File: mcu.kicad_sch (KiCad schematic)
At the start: 0 parts

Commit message: feat(mcu): Add STM32F030F4Px microcontroller to schematic
This commit adds the STM32F030F4Px microcontroller to the `mcu.kicad_sch`
schematic sheet.

- Added the STM32F030F4Px symbol.
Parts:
- added U2: STM32F030F4Px, Package_SO:TSSOP-20_4.4x6.5mm_P0.65mm, symbol MCU_ST_STM32F0:STM32F030F4Px
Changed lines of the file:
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@@
 	(generator_version "9.0")
 	(paper "A4")
+	(symbol
+		(lib_id "MCU_ST_STM32F0:STM32F030F4Px")
+		(at 154.94 105.41 0)
+		(unit 1)
+		(exclude_from_sim no)
+		(in_bom yes)
+		(on_board yes)
+		(dnp no)
+		(fields_autoplaced yes)
+		(property "Reference" "U2"
+			(at 157.0833 125.73 0)
+			(effects
+				(font
+					(size 1.27 1.27)
+				)
+				(justify left)
+			)
+		)
+		(property "Value" "STM32F030F4Px"
+			(at 157.0833 128.27 0)
+			(effects
+				(font
+					(size 1.27 1.27)
+				)
+				(justify left)
+			)
+		)
+		(property "Footprint" "Package_SO:TSSOP-20_4.4x6.5mm_P0.65mm"
+			(at 144.78 123.19 0)
+			(effects
+				(font
+					(size 1.27 1.27)
+				)
+				(justify right)
+				(hide yes)
+			)
+		)
+		(property "Datasheet" "https://www.st.com/resource/en/datasheet/stm32f030f4.pdf"
+			(at 154.94 105.41 0)
+			(effects
+				(font
+					(size 1.27 1.27)
+				)
+				(hide yes)
+			)
+		)
+		(property "Description" "STMicroelectronics Arm Cortex-M0 MCU, 16KB flash, 4KB RAM, 48 MHz, 2.4-3.6V, 15 GPIO, TSSOP20"
+			(at 154.94 105.41 0)
+			(effects
+				(font
+					(size 1.27 1.27)
+				)
+				(hide yes)
+			)
+		)
+		(pin "6"
+		)
+		(pin "7"
+		)
+		(pin "20"
+		)
+		(pin "19"
+		)
+		(pin "5"
+		)
+		(pin "18"
+		)
+		(pin "13"
+		)
+		(pin "9"
+		)
+		(pin "16"
+		)
+		(pin "15"
+		)
+		(pin "3"
+		)
+		(pin "2"
+		)
+		(pin "1"
+		)
+		(pin "4"
+		)
+		(pin "14"
+		)
+		(pin "11"
+		)
+		(pin "17"
+		)
+		(pin "10"
+		)
+		(pin "12"
+		)
+		(pin "8"
+		)
+		(instances
+			(project ""
+				(path "/01550cd7-b424-469c-925b-c370f3609cd4/edb1e4c3-83a3-4443-aa4b-0e758d3bea47"
+					(reference "U2")
+					(unit 1)
+				)
+			)
+		)
+	)
 )

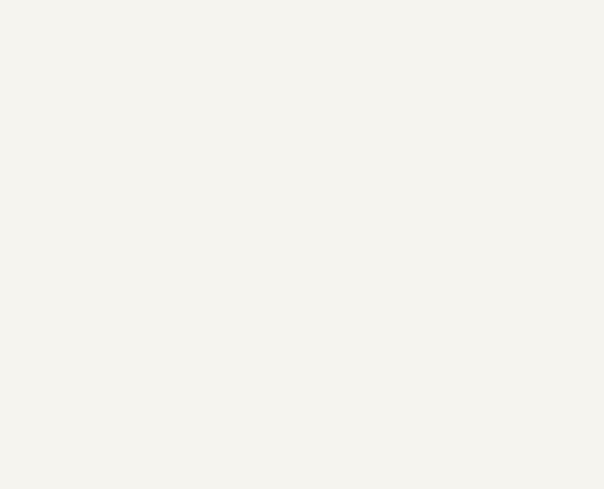
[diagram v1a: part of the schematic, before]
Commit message: feat(power): Added decoupling capacitors for MCU VDD pins
This commit introduces decoupling capacitors on the voltage supply (VDD) pins of
the microcontroller unit (MCU). These capacitors help to stabilize the power
supply by providing a local energy reserve and reducing voltage fluctuations.

This improvement enhances the reliability and stability of the MCU power system,
especially during switching events and periods of high current demand.

Reference

Chapter: 6.1.6 Power supply scheme
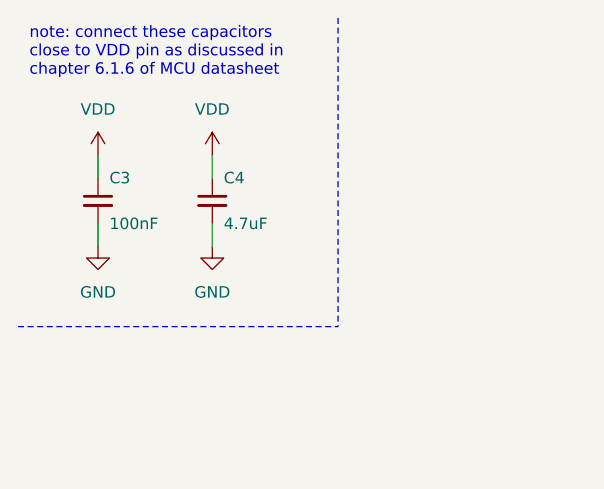
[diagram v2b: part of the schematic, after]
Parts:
- added C3: 100nF, Capacitor_SMD:C_0603_1608Metric_Pad1.08x0.95mm_HandSolder, symbol Device:C_Small
- added C4: 4.7uF, Capacitor_SMD:C_0603_1608Metric_Pad1.08x0.95mm_HandSolder, symbol Device:C_Small
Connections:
- new net GND: C3.2, C4.2
- new net VDD: C3.1, C4.1
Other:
- note added: "note: connect these capacitors close to VDD pin as discussed in chapter 6.1.6 of MCU datasheet"

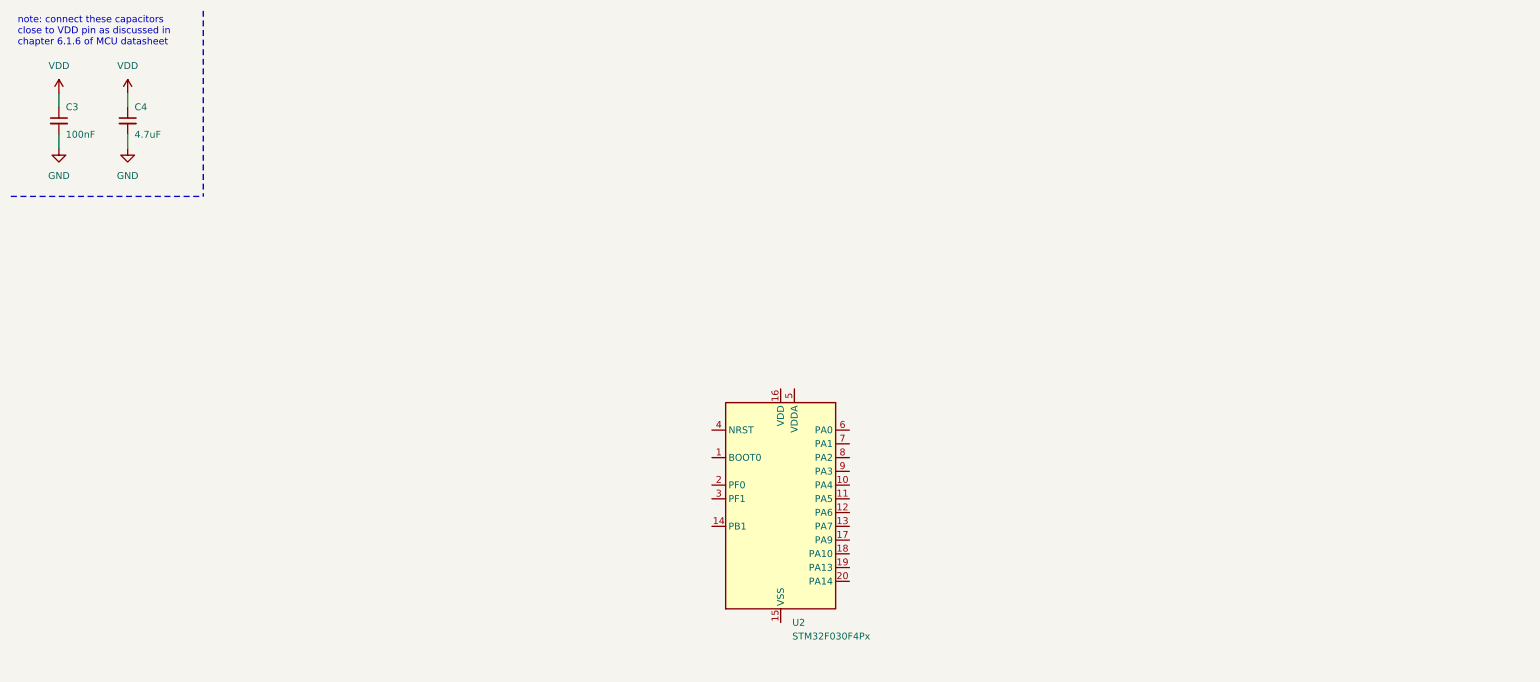
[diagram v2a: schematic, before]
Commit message: feat(power): Added decoupling capacitors for MCU VDDA pins
This commit introduces decoupling capacitors on the analog voltage supply (VDDA)
pins of the microcontroller unit (MCU). Similar to the decoupling for the
digital supply, these capacitors aim to stabilize the analog power rail.

A stable VDDA is crucial for the performance and accuracy of the MCU's analog
peripherals, such as ADCs and DACs. This addition helps to minimize noise and
ensure reliable analog signal processing.

Reference

Chapter: 6.1.6 Power supply scheme
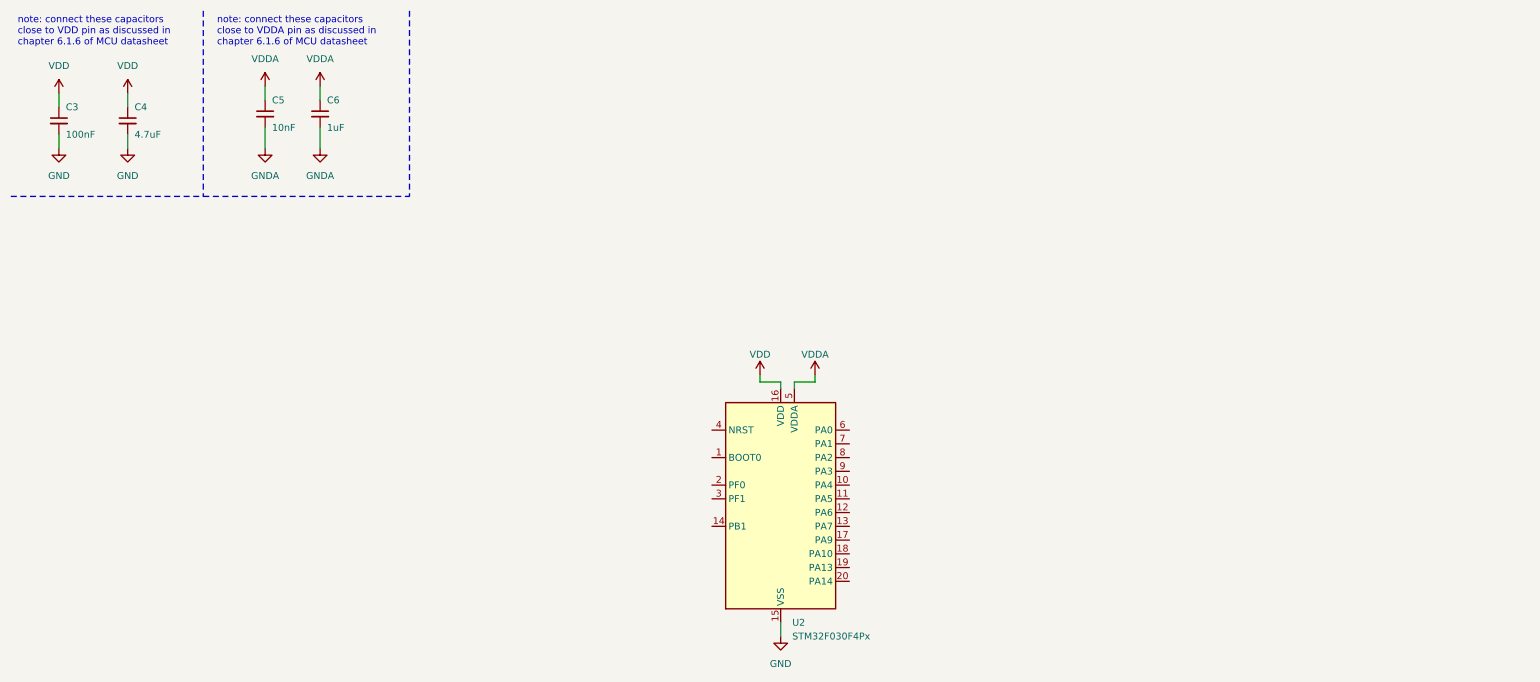
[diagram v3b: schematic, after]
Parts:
- added C5: 10nF, Capacitor_SMD:C_0603_1608Metric_Pad1.08x0.95mm_HandSolder, symbol Device:C_Small
- added C6: 1uF, Capacitor_SMD:C_0603_1608Metric_Pad1.08x0.95mm_HandSolder, symbol Device:C_Small
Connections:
- net GND: now also U2.15 (VSS)
- net VDD: now also U2.16 (VDD)
- net VDDA: now reaches U2.5 (VDDA)
- net VDDA: now also C5.1, C6.1
- new net GNDA: C5.2, C6.2
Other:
- note added: "note: connect these capacitors close to VDDA pin as discussed in chapter 6.1.6 of MCU datasheet"

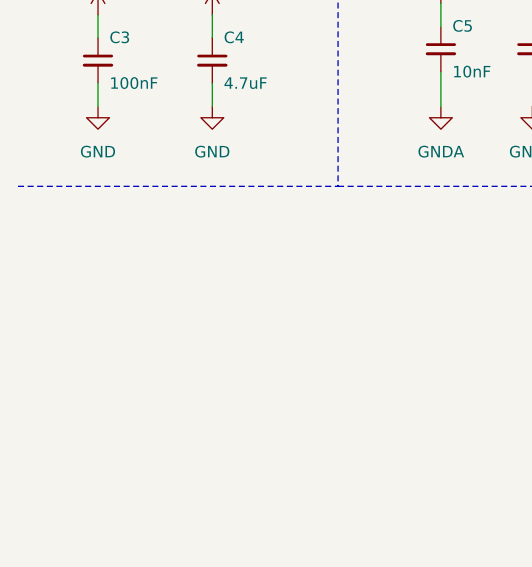
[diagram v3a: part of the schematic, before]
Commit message: fix(power): Connected 3V3_VCC and 3V3_VCCA to VDD and VDDA in MCU
This commit establishes connections between the VCC and VDD pins, as well as
the VCCA and VDDA pins, on the microcontroller unit (MCU).

This resolves a potential issue where the core digital supply (VDD) and the
I/O supply (VCC) were not explicitly linked, and similarly for the analog
supply (VDDA) and analog peripherals supply (VCCA). Connecting these pins
as recommended by the MCU datasheet ensures proper power distribution and
operation of both the digital core and analog peripherals.
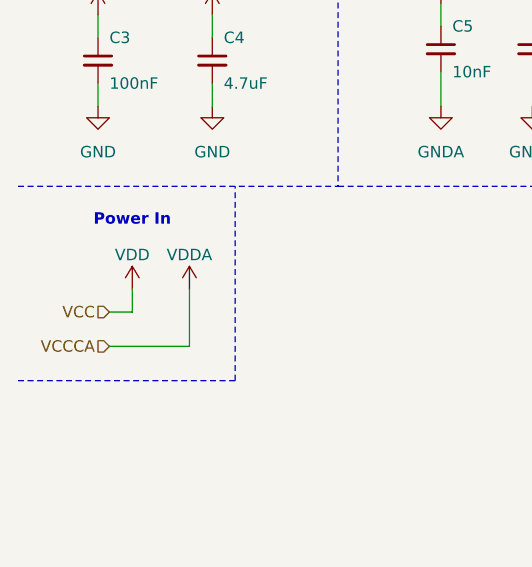
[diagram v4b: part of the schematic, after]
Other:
- note added: "Power In"
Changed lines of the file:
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@@
 				(size 1.27 1.27)
 				(thickness 0.1588)
+				(color 0 0 0 1)
 			)
 			(justify left)
+		)
+	)
+	(text "Power In"
+		(exclude_from_sim no)
+		(at 25.4 50.8 0)
+		(effects
+			(font
+				(size 1.27 1.27)
+				(thickness 0.254)
+				(bold yes)
+				(color 0 0 0 1)
+			)
 		)
 	)
@@
 				(size 1.27 1.27)
 				(thickness 0.1588)
+				(color 0 0 0 1)
 			)
 			(justify left)
@@
 	(wire
 		(pts
-			(xy 34.29 30.48) (xy 34.29 27.94)
-		)
-		(stroke
-			(width 0)
-			(type default)
-		)
-	)
-	(wire
-		(pts
-			(xy 59.69 34.29) (xy 59.69 38.1)
-		)
-		(stroke
-			(width 0)
-			(type default)
-		)
-	)
-	(wire
-		(pts
-			(xy 69.85 26.67) (xy 69.85 29.21)
-		)
-		(stroke
-			(width 0)
-			(type default)
-		)
-	)
-	(wire
-		(pts
-			(xy 59.69 26.67) (xy 59.69 29.21)
-		)
-		(stroke
-			(width 0)
-			(type default)
-		)
-	)
-	(wire
-		(pts
-			(xy 157.48 81.28) (xy 157.48 82.55)
-		)
-		(stroke
-			(width 0)
-			(type default)
-		)
-	)
-	(wire
-		(pts
-			(xy 161.29 80.01) (xy 161.29 81.28)
+			(xy 31.75 64.77) (xy 31.75 58.42)
 		)
 		(stroke
@@
 	(polyline
 		(pts
-			(xy 12.7 46.99) (xy 48.26 46.99)
+			(xy 36.83 68.58) (xy 36.83 46.99)
 		)
 		(stroke
@@
 	(wire
 		(pts
-			(xy 21.59 35.56) (xy 21.59 38.1)
-		)
-		(stroke
-			(width 0)
-			(type default)
-		)
-	)
-	(wire
-		(pts
-			(xy 154.94 128.27) (xy 154.94 125.73)
+			(xy 34.29 30.48) (xy 34.29 27.94)
+		)
+		(stroke
+			(width 0)
+			(type default)
+		)
+	)
+	(wire
+		(pts
+			(xy 59.69 34.29) (xy 59.69 38.1)
+		)
+		(stroke
+			(width 0)
+			(type default)
+		)
+	)
+	(wire
+		(pts
+			(xy 25.4 60.96) (xy 22.86 60.96)
+		)
+		(stroke
+			(width 0)
+			(type default)
+		)
+	)
+	(wire
+		(pts
+			(xy 69.85 26.67) (xy 69.85 29.21)
+		)
+		(stroke
+			(width 0)
+			(type default)
+		)
+	)
+	(wire
+		(pts
+			(xy 59.69 26.67) (xy 59.69 29.21)
+		)
+		(stroke
+			(width 0)
+			(type default)
+		)
+	)
+	(wire
+		(pts
+			(xy 25.4 58.42) (xy 25.4 60.96)
+		)
+		(stroke
+			(width 0)
+			(type default)
+		)
+	)
+	(wire
+		(pts
+			(xy 157.48 81.28) (xy 157.48 82.55)
+		)
+		(stroke
+			(width 0)
+			(type default)
+		)
+	)
+	(wire
+		(pts
+			(xy 161.29 80.01) (xy 161.29 81.28)
 		)
 		(stroke
@@
 	(polyline
 		(pts
-			(xy 48.26 46.99) (xy 86.36 46.99)
+			(xy 12.7 46.99) (xy 48.26 46.99)
 		)
 		(stroke
@@
 	(wire
 		(pts
+			(xy 21.59 35.56) (xy 21.59 38.1)
+		)
+		(stroke
+			(width 0)
+			(type default)
+		)
+	)
+	(wire
+		(pts
+			(xy 22.86 64.77) (xy 31.75 64.77)
+		)
+		(stroke
+			(width 0)
+			(type default)
+		)
+	)
+	(polyline
+		(pts
+			(xy 12.7 68.58) (xy 36.83 68.58)
+		)
+		(stroke
+			(width 0)
+			(type dash)
+			(color 72 72 72 1)
+		)
+	)
+	(wire
+		(pts
+			(xy 154.94 128.27) (xy 154.94 125.73)
+		)
+		(stroke
+			(width 0)
+			(type default)
+		)
+	)
+	(polyline
+		(pts
+			(xy 48.26 46.99) (xy 86.36 46.99)
+		)
+		(stroke
+			(width 0)
+			(type dash)
+			(color 72 72 72 1)
+		)
+	)
+	(wire
+		(pts
 			(xy 151.13 81.28) (xy 154.94 81.28)
 		)
@@
 			(width 0)
 			(type default)
+		)
+	)
+	(hierarchical_label "VCC"
+		(shape input)
+		(at 22.86 60.96 180)
+		(effects
+			(font
+				(size 1.27 1.27)
+			)
+			(justify right)
+		)
+	)
+	(hierarchical_label "VCCCA"
+		(shape input)
+		(at 22.86 64.77 180)
+		(effects
+			(font
+				(size 1.27 1.27)
+			)
+			(justify right)
 		)
 	)
@@
 	)
 	(symbol
+		(lib_id "power:VDDA")
+		(at 31.75 58.42 0)
+		(unit 1)
+		(exclude_from_sim no)
+		(in_bom yes)
+		(on_board yes)
+		(dnp no)
+		(property "Reference" "#PWR016"
+			(at 31.75 62.23 0)
+			(effects
+				(font
+					(size 1.27 1.27)
+				)
+				(hide yes)
+			)
+		)
+		(property "Value" "VDDA"
+			(at 31.75 54.61 0)
+			(effects
+				(font
+					(size 1.27 1.27)
+				)
+			)
+		)
+		(property "Footprint" ""
+			(at 31.75 58.42 0)
+			(effects
+				(font
+					(size 1.27 1.27)
+				)
+				(hide yes)
+			)
+		)
+		(property "Datasheet" ""
+			(at 31.75 58.42 0)
+			(effects
+				(font
+					(size 1.27 1.27)
+				)
+				(hide yes)
+			)
+		)
+		(property "Description" "Power symbol creates a global label with name \"VDDA\""
+			(at 31.75 58.42 0)
+			(effects
+				(font
+					(size 1.27 1.27)
+				)
+				(hide yes)
+			)
+		)
+		(pin "1"
+		)
+		(instances
+			(project ""
+				(path "/01550cd7-b424-469c-925b-c370f3609cd4/edb1e4c3-83a3-4443-aa4b-0e758d3bea47"
+					(reference "#PWR016")
+					(unit 1)
+				)
+			)
+		)
+	)
+	(symbol
 		(lib_id "MCU_ST_STM32F0:STM32F030F4Px")
 		(at 154.94 105.41 0)
@@
 					(unit 1)
 				)
+			)
+		)
+	)
+	(symbol
+		(lib_id "power:VDD")
+		(at 25.4 58.42 0)
+		(unit 1)
+		(exclude_from_sim no)
+		(in_bom yes)
+		(on_board yes)
+		(dnp no)
+		(property "Reference" "#PWR011"
+			(at 25.4 62.23 0)
+			(effects
+				(font
+					(size 1.27 1.27)
+				)
+				(hide yes)
+			)
+		)
+		(property "Value" "VDD"
+			(at 25.4 54.61 0)
+			(effects
+				(font
+					(size 1.27 1.27)
+				)
+			)
+		)
+		(property "Footprint" ""
+			(at 25.4 58.42 0)
+			(effects
+				(font
+					(size 1.27 1.27)
+				)
+				(hide yes)
+			)
+		)
+		(property "Datasheet" ""
+			(at 25.4 58.42 0)
+			(effects
+				(font
+					(size 1.27 1.27)
+				)
+				(hide yes)
+			)
+		)
+		(property "Description" "Power symbol creates a global label with name \"VDD\""
+			(at 25.4 58.42 0)
+			(effects
+				(font
+					(size 1.27 1.27)
+				)
+				(hide yes)
+			)
+		)
+		(pin "1"
+		)
+		(instances
+			(project ""
+				(path "/01550cd7-b424-469c-925b-c370f3609cd4/edb1e4c3-83a3-4443-aa4b-0e758d3bea47"
+					(reference "#PWR011")
+					(unit 1)
+				)

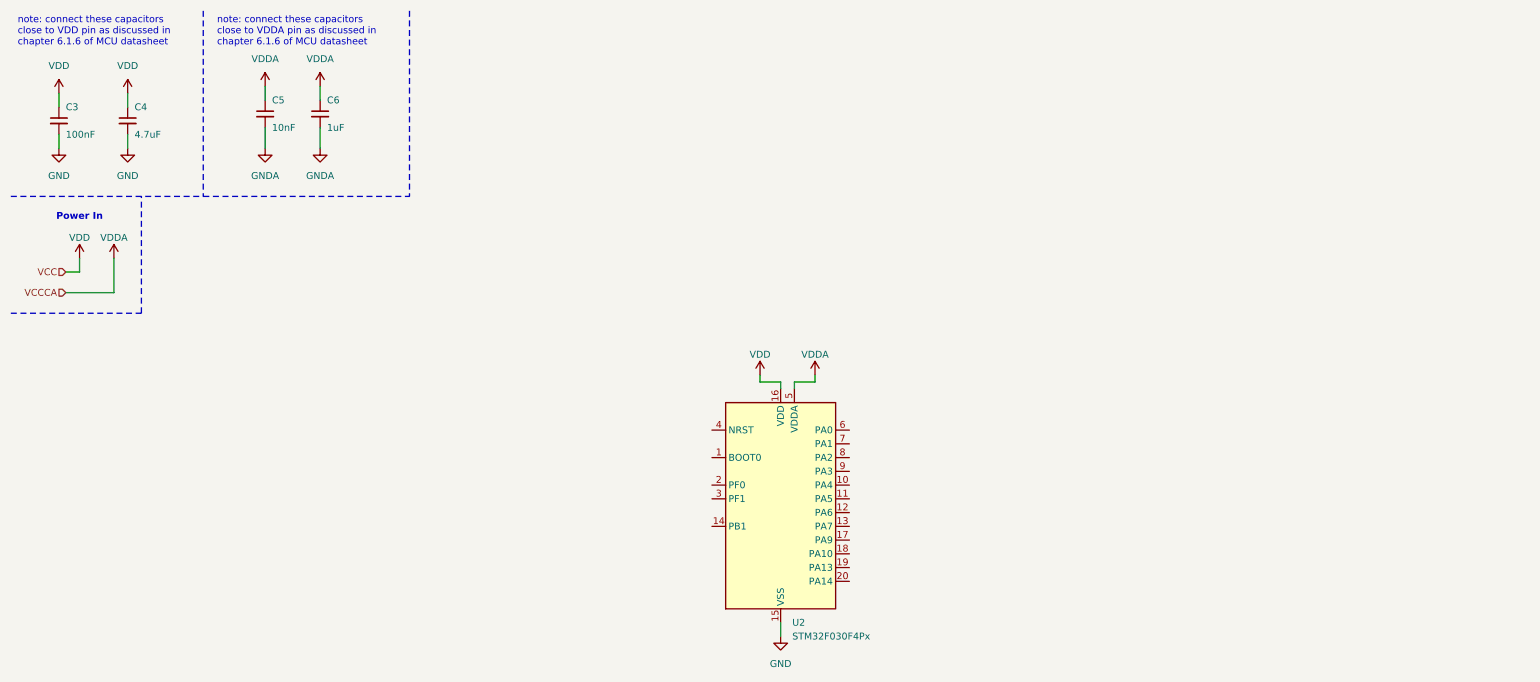
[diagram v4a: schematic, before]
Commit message: feat(mcu): Add NRST reset circuitry for MCU
Implements the reset circuitry for the microcontroller's NRST pin in the schematic.

This includes:
- Placement of the reset button (if newly added in this step).
- External capacitor for protection from parasitic reset
- Connection to the MCU's NRST pin.

This ensures a reliable method for hardware resetting the microcontroller, clearly documented within the schematic.
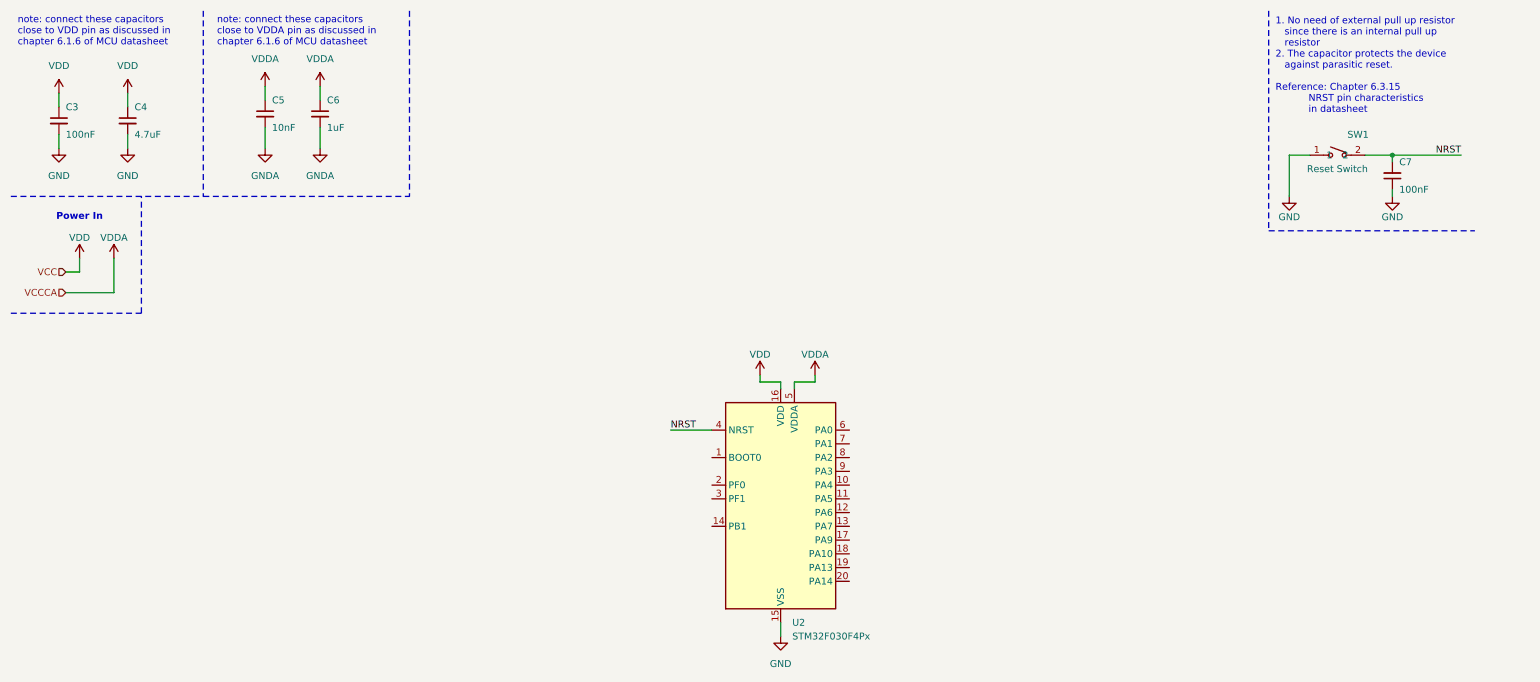
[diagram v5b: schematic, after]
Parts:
- added C7: 100nF, Capacitor_SMD:C_0805_2012Metric_Pad1.18x1.45mm_HandSolder, symbol Device:C_Small
- added SW1: Reset Switch, lcsc:BZCN_TSB008A2530A, symbol lcsc_switch:TSB008A2530A
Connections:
- net GND: now also C7.1, SW1.1
- net NRST: now reaches U2.4 (NRST)
- net NRST: now also C7.2, SW1.2
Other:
- note added: "1. No need of external pull up resistor since there is an internal pull up resistor 2. The capacitor protects the device against parasitic reset. Reference: Chapter 6.3.15 NRST pin characteristics in datasheet"
